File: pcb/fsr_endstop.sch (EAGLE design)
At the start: 33 parts, among them U1 ATTINY461

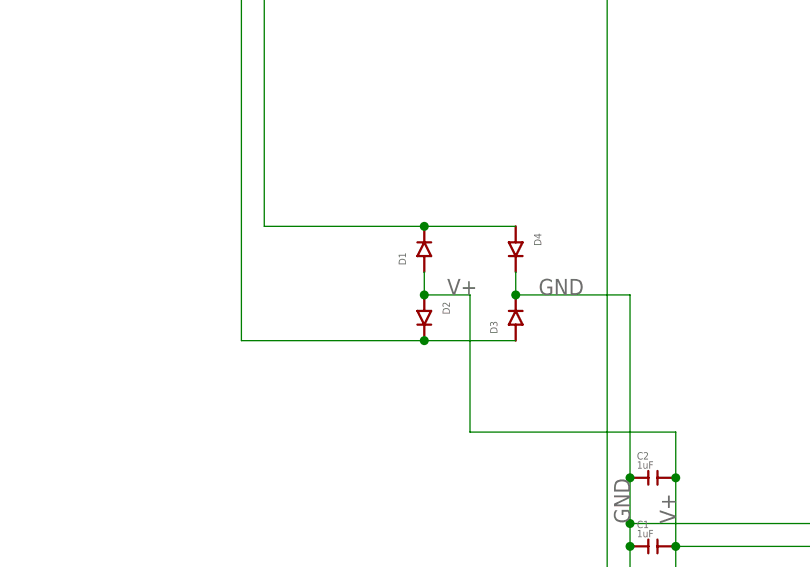
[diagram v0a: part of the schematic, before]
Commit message: Reverse polarity of diodes
Diodes were backwards in the schematic for the bridge rectifier.
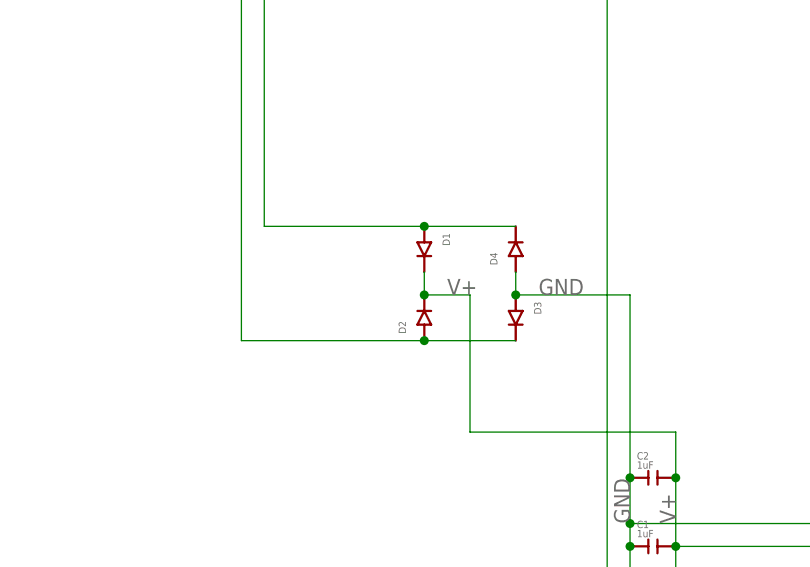
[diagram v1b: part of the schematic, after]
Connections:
- removed net N$4: +/-.P$1, D1.-, D4.+
- new net N$24: +/-.P$1, D1.+, D4.-
- net GND: now also D3.+, D4.+; no longer D3.-, D4.-
- net N$3: now also D2.+, D3.-; no longer D2.-, D3.+
- net V+: now also D1.-, D2.-; no longer D1.+, D2.+
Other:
- moved on the sheet: D1, D2, D3, D4
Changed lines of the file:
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@@
 <instance part="FSR3A" gate="G$1" x="129.54" y="88.9" rot="R270"/>
 <instance part="AVR1" gate="G$1" x="50.8" y="10.16" rot="R90"/>
-<instance part="D1" gate="G$1" x="20.32" y="111.76" rot="R90"/>
-<instance part="D2" gate="G$1" x="20.32" y="104.14" rot="R270"/>
-<instance part="D3" gate="G$1" x="30.48" y="104.14" rot="R90"/>
-<instance part="D4" gate="G$1" x="30.48" y="111.76" rot="R270"/>
+<instance part="D1" gate="G$1" x="20.32" y="111.76" rot="R270"/>
+<instance part="D2" gate="G$1" x="20.32" y="104.14" rot="R90"/>
+<instance part="D3" gate="G$1" x="30.48" y="104.14" rot="R270"/>
+<instance part="D4" gate="G$1" x="30.48" y="111.76" rot="R90"/>
 <instance part="C1" gate="G$1" x="45.72" y="78.74"/>
 <instance part="LED1" gate="G$1" x="190.5" y="43.18"/>
@@
 <net name="N$3" class="0">
 <segment>
-<pinref part="D3" gate="G$1" pin="+"/>
-<pinref part="D2" gate="G$1" pin="-"/>
-<wire x1="30.48" y1="101.6" x2="20.32" y2="101.6" width="0.1524" layer="91"/>
-<wire x1="20.32" y1="101.6" x2="0" y2="101.6" width="0.1524" layer="91"/>
 <wire x1="0" y1="101.6" x2="0" y2="152.4" width="0.1524" layer="91"/>
-<junction x="20.32" y="101.6"/>
 <pinref part="-/+" gate="G$1" pin="P$1"/>
 <wire x1="0" y1="152.4" x2="-12.7" y2="152.4" width="0.1524" layer="91"/>
-</segment>
-</net>
-<net name="N$4" class="0">
-<segment>
-<pinref part="+/-" gate="G$1" pin="P$1"/>
-<wire x1="-12.7" y1="162.56" x2="2.54" y2="162.56" width="0.1524" layer="91"/>
-<wire x1="2.54" y1="162.56" x2="2.54" y2="114.3" width="0.1524" layer="91"/>
-<pinref part="D1" gate="G$1" pin="-"/>
-<wire x1="2.54" y1="114.3" x2="20.32" y2="114.3" width="0.1524" layer="91"/>
-<pinref part="D4" gate="G$1" pin="+"/>
-<wire x1="20.32" y1="114.3" x2="30.48" y2="114.3" width="0.1524" layer="91"/>
-<junction x="20.32" y="114.3"/>
+<pinref part="D2" gate="G$1" pin="+"/>
+<wire x1="20.32" y1="101.6" x2="0" y2="101.6" width="0.1524" layer="91"/>
+<pinref part="D3" gate="G$1" pin="-"/>
+<wire x1="20.32" y1="101.6" x2="30.48" y2="101.6" width="0.1524" layer="91"/>
+<junction x="20.32" y="101.6"/>
 </segment>
 </net>
 <net name="V+" class="0">
 <segment>
-<pinref part="D2" gate="G$1" pin="+"/>
-<pinref part="D1" gate="G$1" pin="+"/>
-<wire x1="20.32" y1="106.68" x2="20.32" y2="109.22" width="0.1524" layer="91"/>
-<wire x1="20.32" y1="106.68" x2="25.4" y2="106.68" width="0.1524" layer="91"/>
-<junction x="20.32" y="106.68"/>
 <wire x1="25.4" y1="106.68" x2="25.4" y2="91.44" width="0.1524" layer="91"/>
 <pinref part="U1" gate="G$1" pin="15_AVCC"/>
@@
 <junction x="48.26" y="78.74"/>
 <label x="48.26" y="81.28" size="1.778" layer="95" rot="R90"/>
-<label x="22.86" y="106.68" size="1.778" layer="95"/>
 <wire x1="48.26" y1="86.36" x2="48.26" y2="78.74" width="0.1524" layer="91"/>
 <wire x1="48.26" y1="35.56" x2="48.26" y2="20.32" width="0.1524" layer="91"/>
@@
 <pinref part="C2" gate="G$1" pin="P$2"/>
 <junction x="48.26" y="86.36"/>
+<pinref part="D1" gate="G$1" pin="-"/>
+<pinref part="D2" gate="G$1" pin="-"/>
+<wire x1="20.32" y1="109.22" x2="20.32" y2="106.68" width="0.1524" layer="91"/>
+<wire x1="20.32" y1="106.68" x2="25.4" y2="106.68" width="0.1524" layer="91"/>
+<junction x="20.32" y="106.68"/>
+<label x="22.86" y="106.68" size="1.778" layer="95"/>
 </segment>
 </net>
 <net name="GND" class="0">
 <segment>
-<pinref part="D4" gate="G$1" pin="-"/>
-<pinref part="D3" gate="G$1" pin="-"/>
-<wire x1="30.48" y1="109.22" x2="30.48" y2="106.68" width="0.1524" layer="91"/>
 <pinref part="C1" gate="G$1" pin="P$1"/>
 <wire x1="43.18" y1="78.74" x2="43.18" y2="58.42" width="0.1524" layer="91"/>
@@
 <wire x1="43.18" y1="33.02" x2="43.18" y2="58.42" width="0.1524" layer="91"/>
 <junction x="43.18" y="58.42"/>
-<wire x1="30.48" y1="106.68" x2="43.18" y2="106.68" width="0.1524" layer="91"/>
 <wire x1="43.18" y1="106.68" x2="43.18" y2="86.36" width="0.1524" layer="91"/>
-<junction x="30.48" y="106.68"/>
 <junction x="43.18" y="78.74"/>
 <label x="43.18" y="81.28" size="1.778" layer="95" rot="R90"/>
@@
 <pinref part="C2" gate="G$1" pin="P$1"/>
 <junction x="43.18" y="86.36"/>
+<pinref part="D4" gate="G$1" pin="+"/>
+<pinref part="D3" gate="G$1" pin="+"/>
+<wire x1="30.48" y1="109.22" x2="30.48" y2="106.68" width="0.1524" layer="91"/>
+<wire x1="30.48" y1="106.68" x2="43.18" y2="106.68" width="0.1524" layer="91"/>
+<junction x="30.48" y="106.68"/>
 </segment>
 </net>
@@
 </segment>
 </net>
+<net name="N$24" class="0">
+<segment>
+<pinref part="D4" gate="G$1" pin="-"/>
+<pinref part="D1" gate="G$1" pin="+"/>
+<wire x1="30.48" y1="114.3" x2="20.32" y2="114.3" width="0.1524" layer="91"/>
+<pinref part="+/-" gate="G$1" pin="P$1"/>
+<wire x1="-12.7" y1="162.56" x2="2.54" y2="162.56" width="0.1524" layer="91"/>
+<wire x1="2.54" y1="162.56" x2="2.54" y2="114.3" width="0.1524" layer="91"/>
+<wire x1="20.32" y1="114.3" x2="2.54" y2="114.3" width="0.1524" layer="91"/>
+<junction x="20.32" y="114.3"/>
+</segment>
+</net>
